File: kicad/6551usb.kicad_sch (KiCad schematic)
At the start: 41 parts, among them J1 Conn_01x03_Male, P1 DLP-USB245R, SW1 SW_DIP_x06, U1 74LS04, U10 74LS74, U11 74LS86, U12 74LS33, U13 74LS273, U14 74LS374, U15 74LS244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

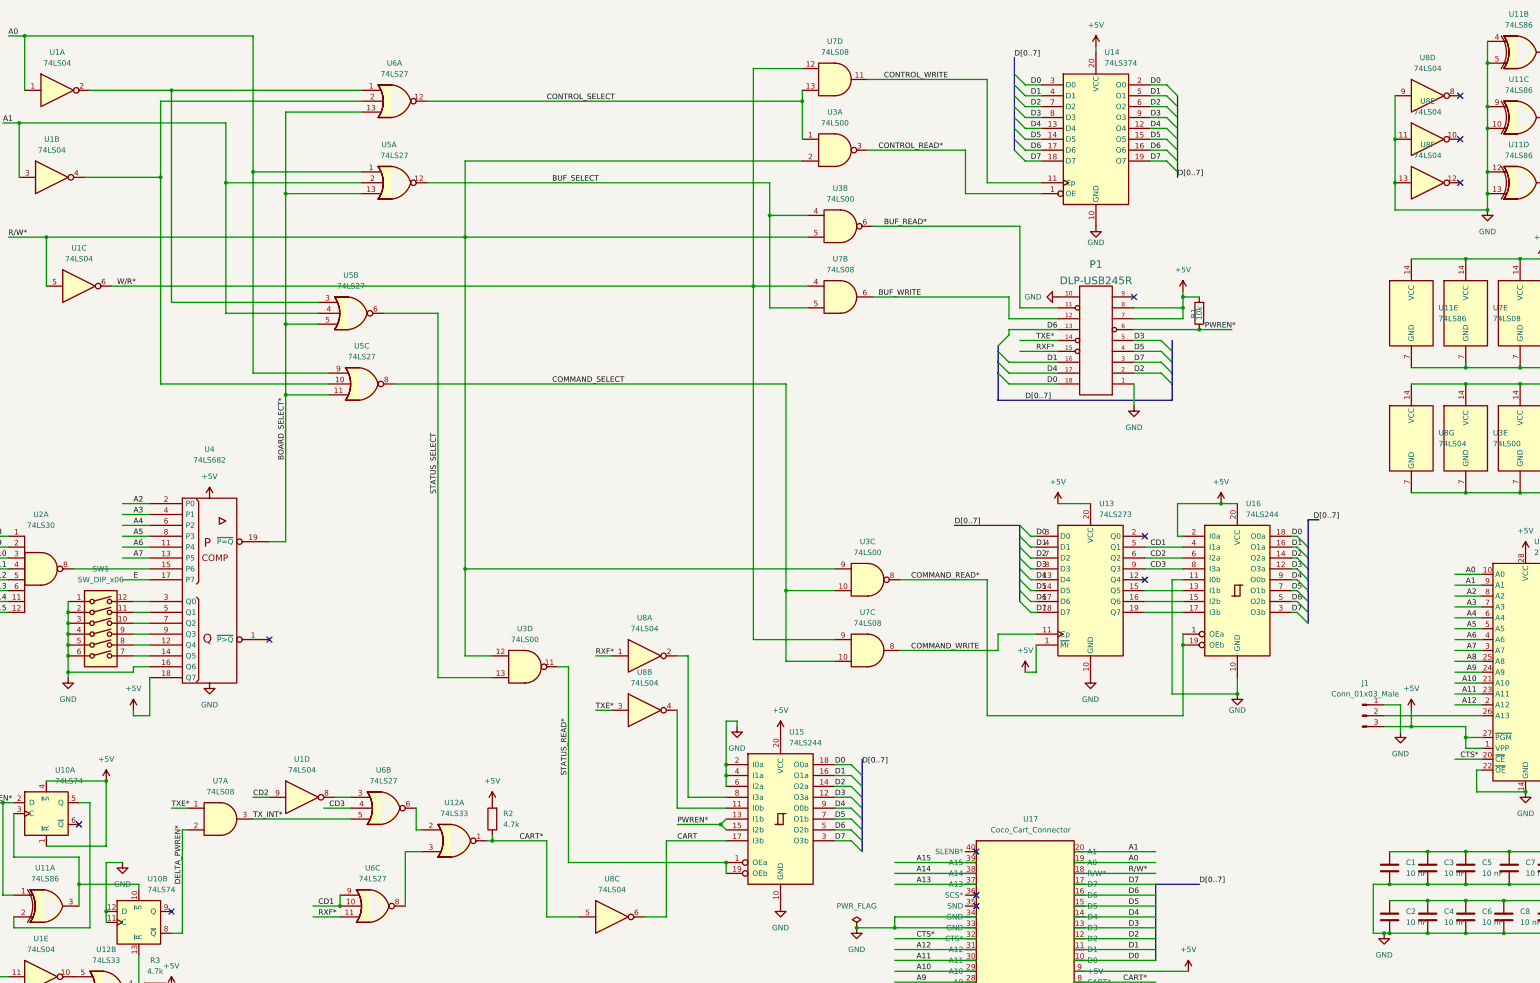
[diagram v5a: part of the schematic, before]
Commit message: Updated for correct logic on PWREN second flipflop
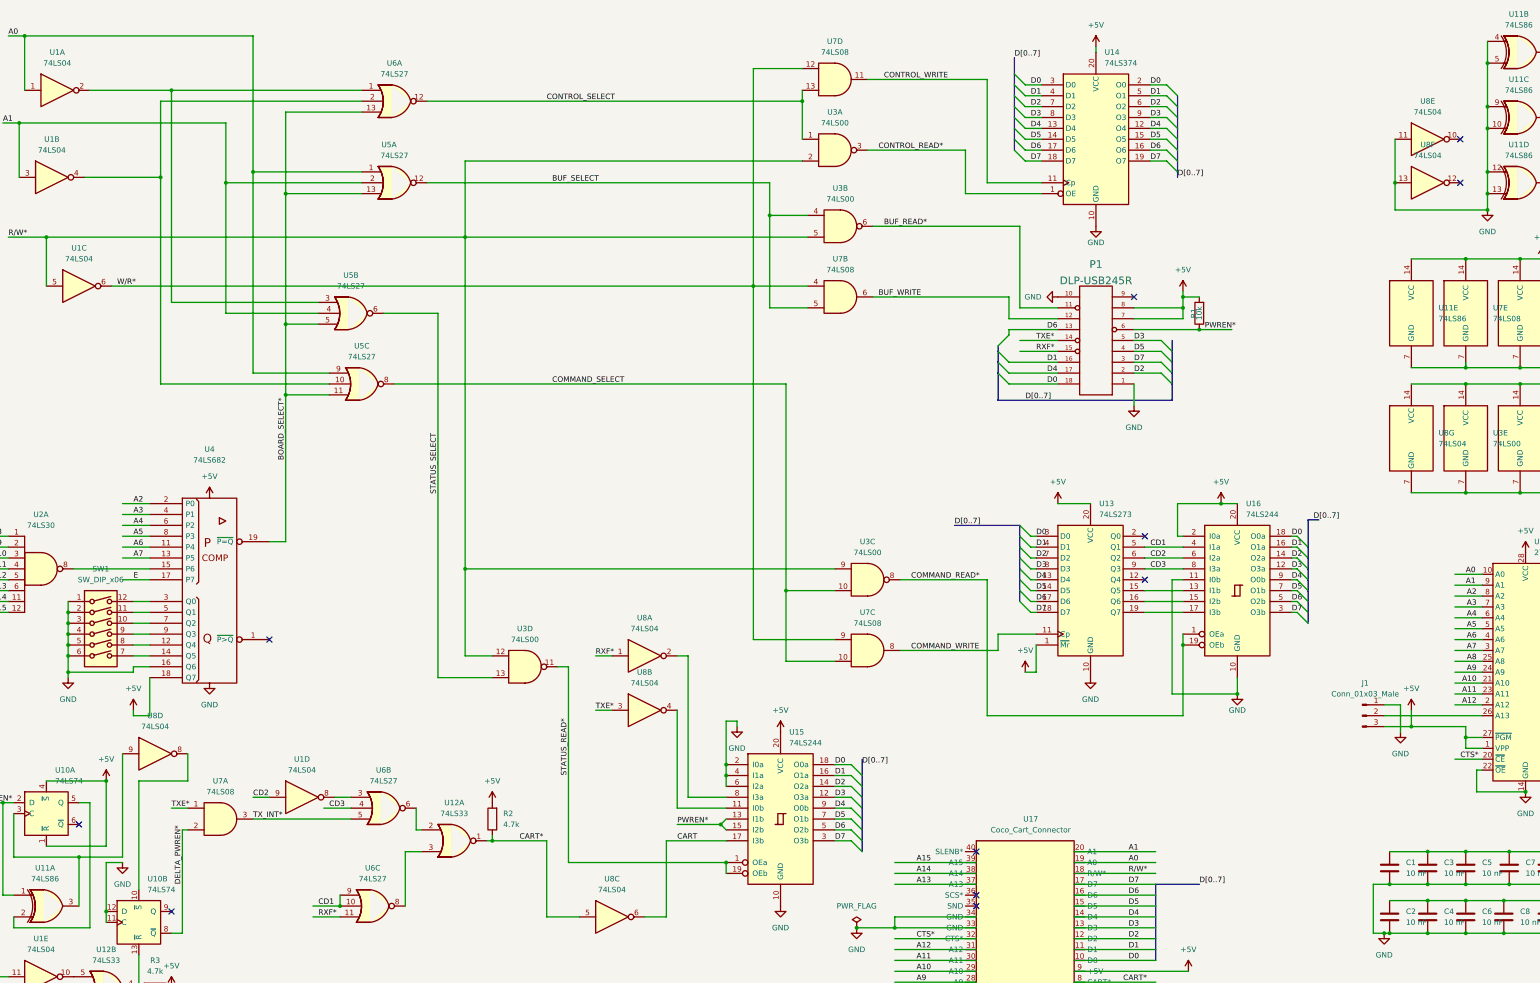
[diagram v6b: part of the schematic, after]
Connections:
- net GND: no longer U8.9
- net at U8.8: now also U10.10 (~{S})
- net at U10.3 (C), U11.3: now also U8.9; no longer U10.10 (~{S})
- no-connect marks 21 -> 20
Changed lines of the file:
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@@
   (junction (at 354.33 217.17) (diameter 0) (color 0 0 0 0)
   )
-  (junction (at 346.71 43.18) (diameter 0) (color 0 0 0 0)
-  )
   (junction (at 297.18 80.01) (diameter 0) (color 0 0 0 0)
   )
@@
   (junction (at 309.88 172.72) (diameter 0) (color 0 0 0 0)
   )
+  (junction (at 39.37 210.82) (diameter 0) (color 0 0 0 0)
+  )
   (junction (at 372.11 228.6) (diameter 0) (color 0 0 0 0)
   )
@@
   (junction (at 394.97 96.52) (diameter 0) (color 0 0 0 0)
   )
-  (junction (at 39.37 217.17) (diameter 0) (color 0 0 0 0)
-  )
   (junction (at 368.3 25.4) (diameter 0) (color 0 0 0 0)
   )
@@
   (no_connect (at 60.96 223.52))
   (no_connect (at 361.95 53.34))
-  (no_connect (at 361.95 33.02))
   (no_connect (at 361.95 43.18))
   (no_connect (at 83.82 160.02))
@@
     (stroke (width 0) (type default) (color 0 0 0 0))
   )
+  (wire (pts (xy 49.53 186.69) (xy 49.53 210.82))
+    (stroke (width 0) (type default) (color 0 0 0 0))
+  )
   (wire (pts (xy 363.22 71.12) (xy 375.92 71.12))
     (stroke (width 0) (type default) (color 0 0 0 0))
@@
     (stroke (width 0) (type default) (color 0 0 0 0))
   )
-  (wire (pts (xy 346.71 33.02) (xy 346.71 43.18))
-    (stroke (width 0) (type default) (color 0 0 0 0))
-  )
   (wire (pts (xy 251.46 146.05) (xy 251.46 177.8))
     (stroke (width 0) (type default) (color 0 0 0 0))
@@
     (stroke (width 0) (type default) (color 0 0 0 0))
   )
+  (wire (pts (xy 64.77 193.04) (xy 53.34 193.04))
+    (stroke (width 0) (type default) (color 0 0 0 0))
+  )
   (bus (pts (xy 393.7 138.43) (xy 396.24 138.43))
     (stroke (width 0) (type default) (color 0 0 0 0))
@@
     (stroke (width 0) (type default) (color 0 0 0 0))
   )
-  (wire (pts (xy 39.37 217.17) (xy 39.37 210.82))
+  (wire (pts (xy 39.37 210.82) (xy 39.37 222.25))
     (stroke (width 0) (type default) (color 0 0 0 0))
   )
@@
     (stroke (width 0) (type default) (color 0 0 0 0))
   )
-  (wire (pts (xy 39.37 222.25) (xy 39.37 217.17))
-    (stroke (width 0) (type default) (color 0 0 0 0))
-  )
   (wire (pts (xy 344.17 175.26) (xy 347.98 175.26))
     (stroke (width 0) (type default) (color 0 0 0 0))
@@
     (stroke (width 0) (type default) (color 0 0 0 0))
   )
+  (wire (pts (xy 39.37 210.82) (xy 49.53 210.82))
+    (stroke (width 0) (type default) (color 0 0 0 0))
+  )
   (wire (pts (xy 294.64 172.72) (xy 309.88 172.72))
     (stroke (width 0) (type default) (color 0 0 0 0))
@@
     (stroke (width 0) (type default) (color 0 0 0 0))
   )
-  (wire (pts (xy 53.34 217.17) (xy 53.34 218.44))
+  (wire (pts (xy 53.34 193.04) (xy 53.34 218.44))
     (stroke (width 0) (type default) (color 0 0 0 0))
   )
@@
     (stroke (width 0) (type default) (color 0 0 0 0))
   )
-  (wire (pts (xy 39.37 217.17) (xy 53.34 217.17))
-    (stroke (width 0) (type default) (color 0 0 0 0))
-  )
   (wire (pts (xy 55.88 168.91) (xy 55.88 177.8))
     (stroke (width 0) (type default) (color 0 0 0 0))
@@
     (stroke (width 0) (type default) (color 0 0 0 0))
   )
+  (wire (pts (xy 64.77 186.69) (xy 64.77 193.04))
+    (stroke (width 0) (type default) (color 0 0 0 0))
+  )
   (wire (pts (xy 264.16 55.88) (xy 246.38 55.88))
     (stroke (width 0) (type default) (color 0 0 0 0))
@@
     (pin "2")
   )
-  (symbol (lib_id "74xx:74LS04") (at 354.33 33.02 0) (unit 4)
-    (in_bom yes) (on_board yes) (fields_autoplaced)
-    (property "Reference" "U8" (id 0) (at 354.33 24.13 0))
-    (property "Value" "74LS04" (id 1) (at 354.33 26.67 0))
-    (property "Footprint" "Package_DIP:DIP-14_W7.62mm" (id 2) (at 354.33 33.02 0)
-      (effects (font (size 1.27 1.27)) hide)
-    )
-    (property "Datasheet" "http://www.ti.com/lit/gpn/sn74LS04" (id 3) (at 354.33 33.02 0)
-      (effects (font (size 1.27 1.27)) hide)
-    )
-    (pin "1")
-    (pin "2")
-    (pin "3")
-    (pin "4")
-    (pin "5")
-    (pin "6")
-    (pin "8")
-    (pin "9")
-    (pin "10")
-    (pin "11")
-    (pin "12")
-    (pin "13")
-    (pin "14")
-    (pin "7")
-  )
   (symbol (lib_id "power:GND") (at 401.32 29.21 0) (unit 1)
     (in_bom yes) (on_board yes) (fields_autoplaced)
@@
   (symbol (lib_id "power:+5V") (at 45.72 193.04 0) (unit 1)
     (in_bom yes) (on_board yes) (fields_autoplaced)
-    (property "Reference" "#PWR?" (id 0) (at 45.72 196.85 0)
+    (property "Reference" "#PWR0130" (id 0) (at 45.72 196.85 0)
       (effects (font (size 1.27 1.27)) hide)
     )
@@
     (pin "1")
   )
+  (symbol (lib_id "74xx:74LS04") (at 57.15 186.69 0) (unit 4)
+    (in_bom yes) (on_board yes) (fields_autoplaced)
+    (property "Reference" "U8" (id 0) (at 57.15 177.8 0))
+    (property "Value" "74LS04" (id 1) (at 57.15 180.34 0))
+    (property "Footprint" "Package_DIP:DIP-14_W7.62mm" (id 2) (at 57.15 186.69 0)
+      (effects (font (size 1.27 1.27)) hide)
+    )
+    (property "Datasheet" "http://www.ti.com/lit/gpn/sn74LS04" (id 3) (at 57.15 186.69 0)
+      (effects (font (size 1.27 1.27)) hide)
+    )
+    (pin "1")
+    (pin "2")
+    (pin "3")
+    (pin "4")
+    (pin "5")
+    (pin "6")
+    (pin "8")
+    (pin "9")
+    (pin "10")
+    (pin "11")
+    (pin "12")
+    (pin "13")
+    (pin "14")
+    (pin "7")
+  )
   (symbol (lib_id "74xx:74LS86") (at 375.92 38.1 0) (unit 3)
     (in_bom yes) (on_board yes) (fields_autoplaced)
@@
     )
     (path "/513125ae-da41-4e42-a192-a4b760568210"
-      (reference "#PWR?") (unit 1) (value "+5V") (footprint "")
+      (reference "#PWR0130") (unit 1) (value "+5V") (footprint "")
     )
     (path "/92900cd0-548c-482b-a1b2-9ce27355b8a5"
@@
       (reference "U8") (unit 3) (value "74LS04") (footprint "Package_DIP:DIP-14_W7.62mm")
     )
-    (path "/1e694a9b-8334-4ef9-912d-2219ae0c2f6e"
+    (path "/be1017f6-b6a3-46c7-81c8-f746f89fe347"
       (reference "U8") (unit 4) (value "74LS04") (footprint "Package_DIP:DIP-14_W7.62mm")
     )

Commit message: Updated to 1.06
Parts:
- removed R4: 4.7k, Resistor_THT:R_Axial_DIN0207_L6.3mm_D2.5mm_P7.62mm_Horizontal, symbol Device:R
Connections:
- net GND: now also U1.13, U12.8, U12.9
- net R/W*: no longer U12.8
- net STATUS_SELECT: now also U12.6; no longer U1.13
- net at U1.12: no longer U12.9
- net STATUS_WRITE: no longer names the net of U12.10
- net STATUS_WRITE: no longer U12.6
- no-connect marks 20 -> 22
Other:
- moved on the sheet: U12C, U12D, U1F
